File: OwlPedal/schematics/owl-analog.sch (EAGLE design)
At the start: 73 parts, among them IC1 MCP6040, J1 POWER_JACKPTH, J2 NEUTRIK_NMJ6HCD2, J3 NEUTRIK_NMJ6HCD2, J4 NEUTRIK_NMJ6HCD2, J5 NEUTRIK_NMJ6HCD2, J6 NEUTRIK_NMJ6HCD2, Q1 BS170, T1 2N3904

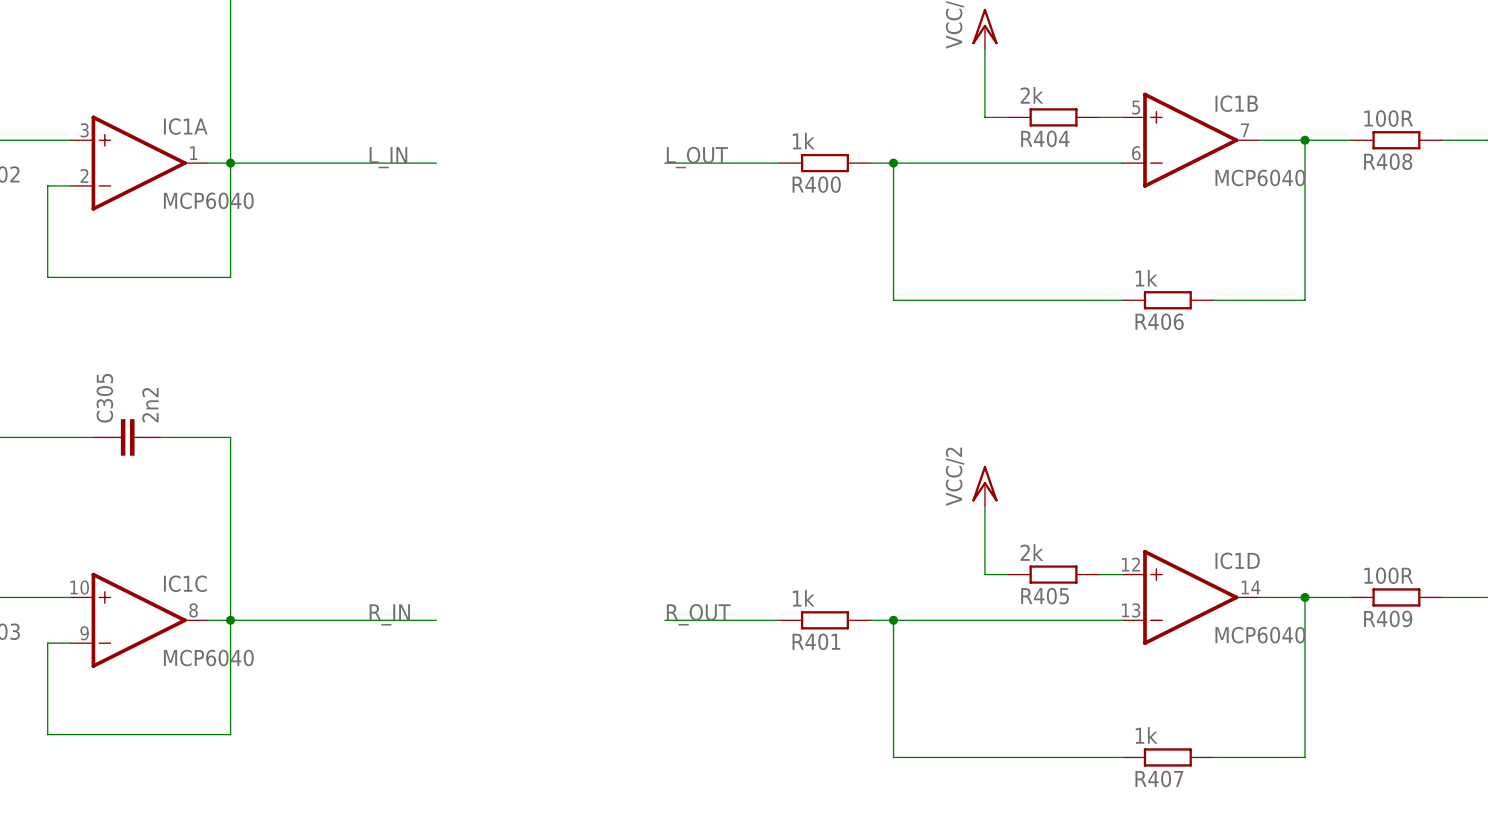
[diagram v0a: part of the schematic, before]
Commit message: changed op amp value to MCP6024
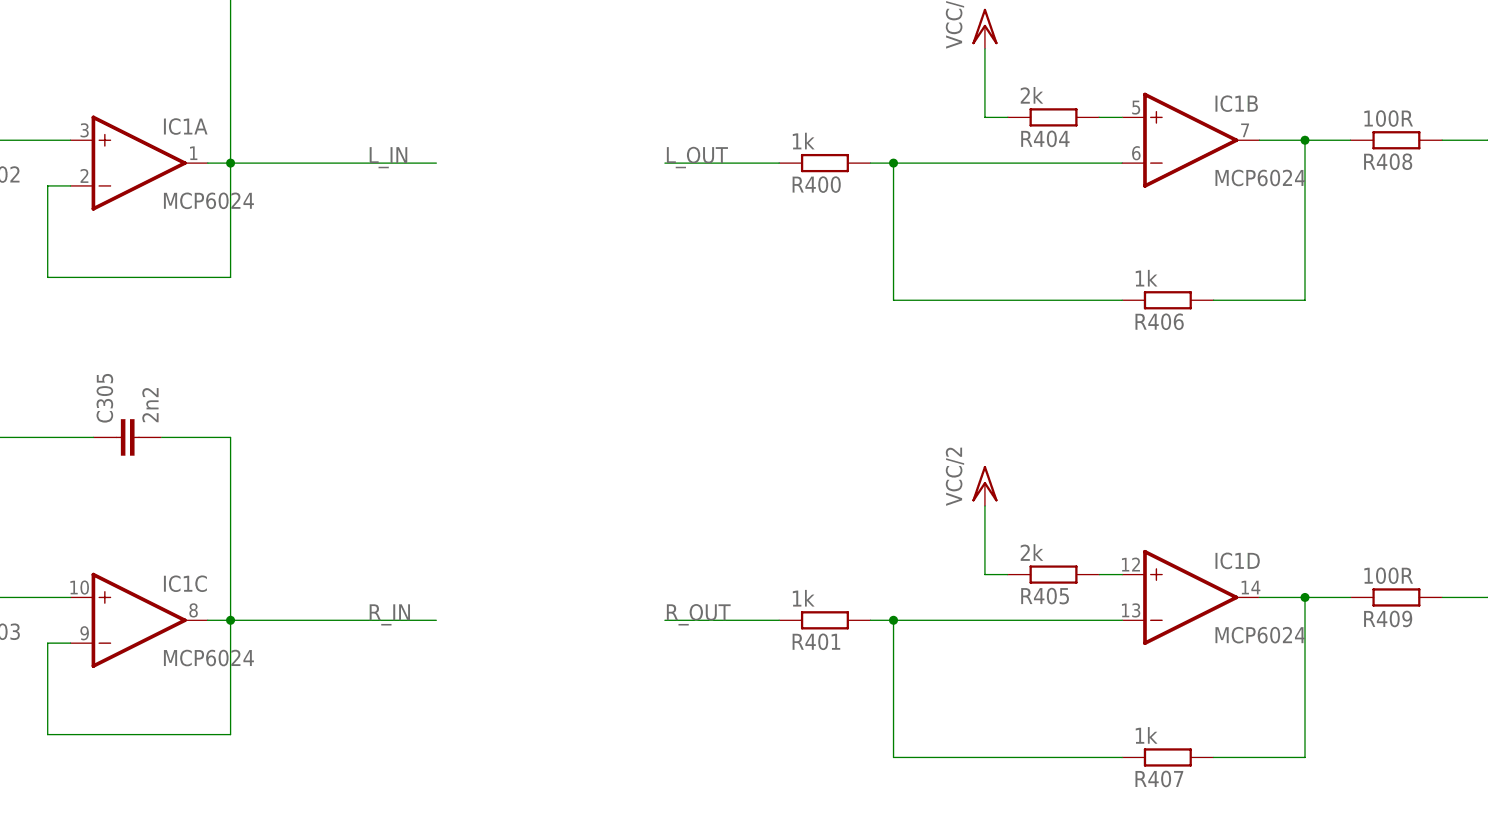
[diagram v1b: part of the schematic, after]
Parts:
- IC1: value MCP6040 -> MCP6024
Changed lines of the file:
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@@
 <part name="P+11" library="supply1" deviceset="VCC/2" device=""/>
 <part name="P+12" library="supply1" deviceset="VCC/2" device=""/>
-<part name="IC1" library="linear" deviceset="TL074" device="P" value="MCP6040"/>
+<part name="IC1" library="linear" deviceset="TL074" device="P" value="MCP6024"/>
 <part name="R406" library="Rebel" deviceset="R-EU_" device="0204/7" value="1k"/>
 <part name="C404" library="capacitor-wima" deviceset="C" device="5/5" value="1uF"/>
